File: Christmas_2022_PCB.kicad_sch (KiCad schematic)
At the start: 32 parts, among them J2 SOP8_test_point, J3 SOP8_test_point

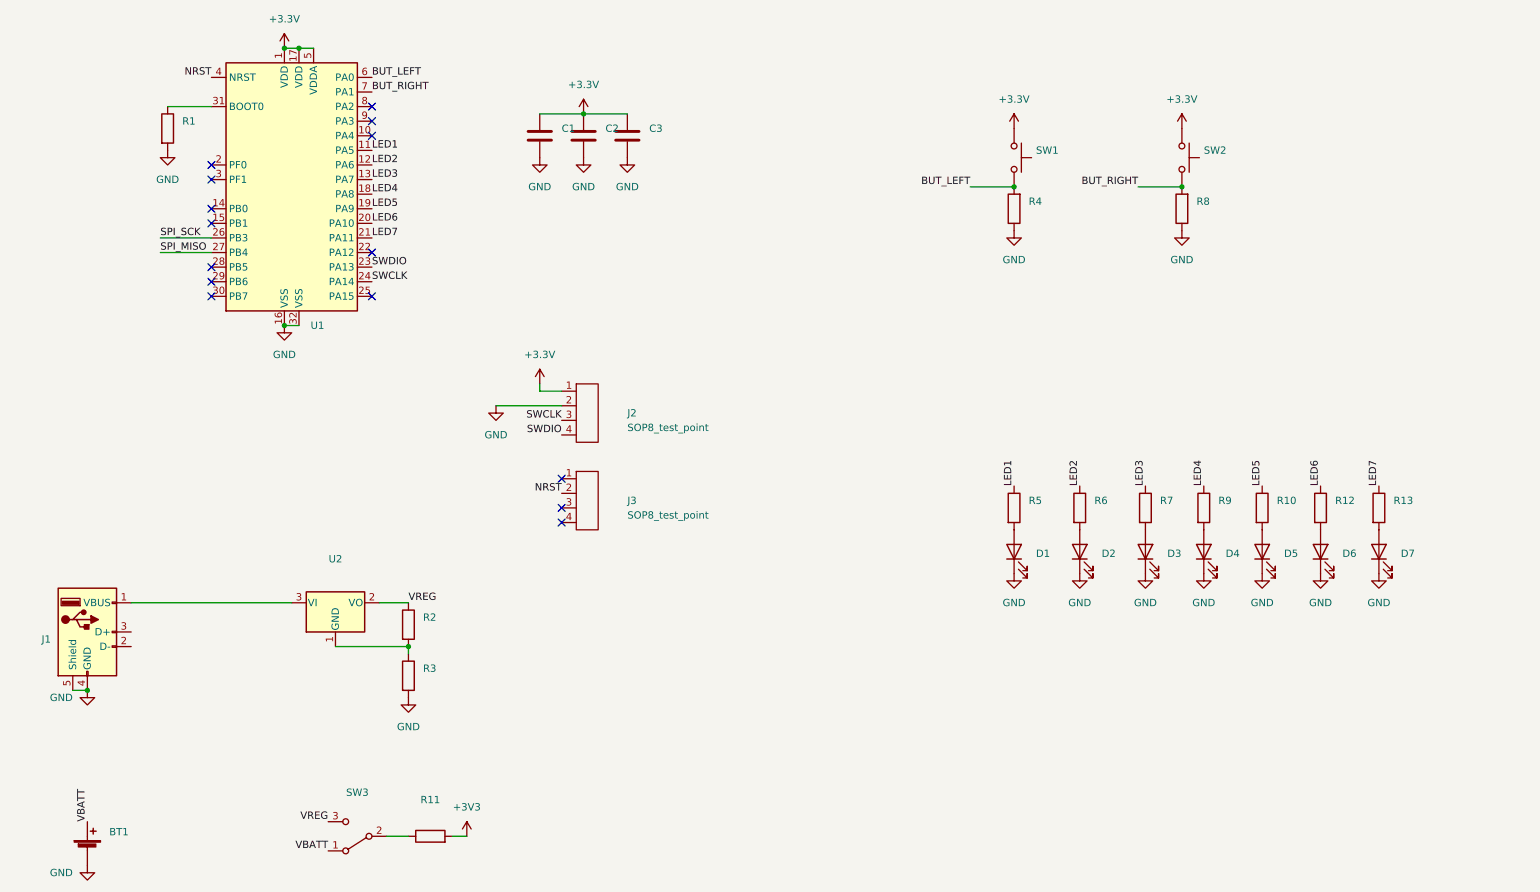
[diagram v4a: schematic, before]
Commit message: Added secondary LEDs
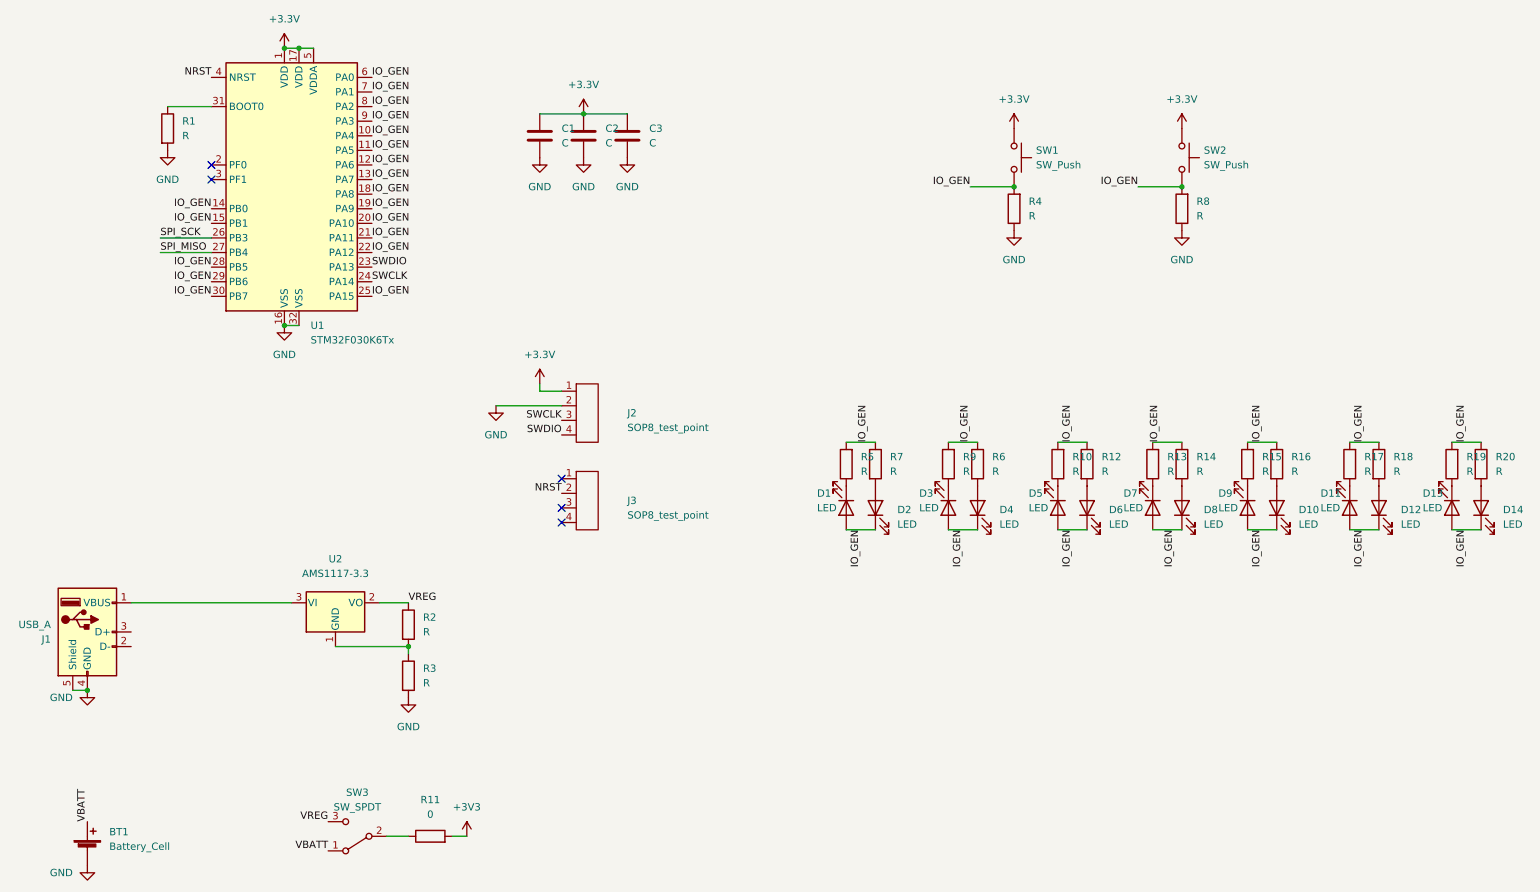
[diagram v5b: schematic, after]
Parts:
- added D10, D11, D12, D13, D14, D8, D9: LED, LED_SMD:LED_0805_2012Metric_Pad1.15x1.40mm_HandSolder, symbol Device:LED
- added R14, R15, R16, R17, R18, R19, R20: R, Resistor_SMD:R_0805_2012Metric_Pad1.20x1.40mm_HandSolder, symbol Device:R
- BT1: value (none) -> Battery_Cell; footprint (none) -> Battery:BatteryHolder_Keystone_3034_1x20mm
- C1, C2, C3: value (none) -> C; footprint (none) -> Capacitor_SMD:C_0805_2012Metric_Pad1.18x1.45mm_HandSolder
- D1, D2, D3, D4, D5, D6, D7: value (none) -> LED; footprint (none) -> LED_SMD:LED_0805_2012Metric_Pad1.15x1.40mm_HandSolder
- J1: value (none) -> USB_A; footprint (none) -> Connector_USB:USB_A_CNCTech_1001-011-01101_Horizontal
- R1, R10, R12, R13, R2, R3, R4, R5, R6, R7, R8, R9: value (none) -> R; footprint (none) -> Resistor_SMD:R_0805_2012Metric_Pad1.20x1.40mm_HandSolder
- R11: value (none) -> 0; footprint (none) -> Resistor_SMD:R_0805_2012Metric_Pad1.20x1.40mm_HandSolder
- SW1, SW2: value (none) -> SW_Push; footprint (none) -> Library:3_6_2_5mm_push_button_G_lead
- SW3: value (none) -> SW_SPDT; footprint (none) -> Button_Switch_SMD:SW_SPDT_PCM12
- U1: value (none) -> STM32F030K6Tx; footprint (none) -> Package_QFP:LQFP-32_7x7mm_P0.8mm
- U2: value (none) -> AMS1117-3.3; footprint (none) -> Package_TO_SOT_SMD:SOT-223-3_TabPin2
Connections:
- net BUT_LEFT is gone; now on net IO_GEN: R4.2, SW1.2, U1.6 (PA0)
- net BUT_RIGHT is gone; now on net IO_GEN: R8.2, SW2.2, U1.7 (PA1)
- net LED2 is gone; now on net IO_GEN: R6.1, U1.12 (PA6)
- net LED3 is gone; now on net IO_GEN: R7.1, U1.13 (PA7)
- net LED6 is gone; now on net IO_GEN: R12.1, U1.20 (PA10)
- net GND: no longer D1.1 (K), D2.1 (K), D3.1 (K), D4.1 (K), D5.1 (K), D6.1 (K), D7.1 (K)
- net at R6.2: now also D4.2 (A); no longer D2.2 (A)
- net IO_GEN: now reaches D5.2 (A), R10.2
- net IO_GEN: now also D1.2 (A), D2.1 (K), D3.2 (A), D4.1 (K), D6.1 (K), D7.2 (A), R13.2, R5.2, R9.2, U1.10 (PA4), U1.11 (PA5), U1.14 (PB0), U1.15 (PB1), U1.18 (PA8), U1.19 (PA9), U1.21 (PA11), U1.22 (PA12), U1.25 (PA15), U1.28 (PB5), U1.29 (PB6), U1.30 (PB7), U1.8 (PA2), U1.9 (PA3), D10.1 (K), D11.2 (A), D12.1 (K), D13.2 (A), D14.1 (K), D8.1 (K), D9.2 (A), R14.1, R15.2, R16.1, R17.2, R18.1, R19.2, R20.1
- net at R7.2: now also D2.2 (A); no longer D3.2 (A)
- net LED1: no longer names the net of R5.1
- net LED1: now also D1.1 (K); no longer U1.11 (PA5)
- net LED4: no longer names the net of R9.1
- net LED4: now also D3.1 (K); no longer U1.18 (PA8)
- net LED5: no longer names the net of R10.1
- net LED5: now also D5.1 (K); no longer U1.19 (PA9)
- net LED7: no longer names the net of R13.1
- net LED7: now also D7.1 (K); no longer U1.21 (PA11)
- new net: D14.2 (A), R20.2
- new net: D10.2 (A), R16.2
- new net: D9.1 (K), R15.1
- new net: D13.1 (K), R19.1
- new net: D11.1 (K), R17.1
- new net: D8.2 (A), R14.2
- new net: D12.2 (A), R18.2
- no-connect marks 15 -> 5

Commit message: finished routing. Added missing 3D models
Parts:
- removed R2, R3: R, Resistor_SMD:R_0805_2012Metric_Pad1.20x1.40mm_HandSolder, symbol Device:R
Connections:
- net GND: now also U2.1 (GND)
- removed net IO_GEN: D1.2 (A), D10.1 (K), D11.2 (A), D12.1 (K), D13.2 (A), D14.1 (K), D2.1 (K), D3.2 (A), D4.1 (K), D5.2 (A), D6.1 (K), D7.2 (A), D8.1 (K), D9.2 (A), R10.2, R12.1, R13.2, R14.1, R15.2, R16.1, R17.2, R18.1, R19.2, R20.1, R4.2, R5.2, R6.1, R7.1, R8.2, R9.2, SW1.2, SW2.2, U1.10 (PA4), U1.11 (PA5), U1.12 (PA6), U1.13 (PA7), U1.14 (PB0), U1.15 (PB1), U1.18 (PA8), U1.19 (PA9), U1.20 (PA10), U1.21 (PA11), U1.22 (PA12), U1.25 (PA15), U1.28 (PB5), U1.29 (PB6), U1.30 (PB7), U1.6 (PA0), U1.7 (PA1), U1.8 (PA2), U1.9 (PA3)
- new net LED1: R5.2, R7.1, U1.21 (PA11)
- new net LED10: D10.1 (K), D9.2 (A), U1.13 (PA7)
- new net LED11: R17.2, R18.1, U1.7 (PA1)
- new net LED12: D11.2 (A), D12.1 (K), U1.6 (PA0)
- new net LED13: R19.2, R20.1, U1.10 (PA4)
- new net LED14: D13.2 (A), D14.1 (K), U1.11 (PA5)
- new net LED2: D1.2 (A), D2.1 (K), U1.22 (PA12)
- new net LED3: R6.1, R9.2, U1.28 (PB5)
- new net LED4: D3.2 (A), D4.1 (K), U1.25 (PA15)
- new net LED5: R10.2, R12.1, U1.15 (PB1)
- new net LED6: D5.2 (A), D6.1 (K), U1.14 (PB0)
- new net LED7: R13.2, R14.1, U1.30 (PB7)
- new net LED8: D7.2 (A), D8.1 (K), U1.29 (PB6)
- new net LED9: R15.2, R16.1, U1.12 (PA6)
- new net SW_LEFT: R4.2, SW1.2, U1.8 (PA2)
- new net SW_RIGHT: R8.2, SW2.2, U1.9 (PA3)
- no-connect marks 5 -> 8

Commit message: Finished routing. Output gerbers and drill files
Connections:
- no-connect marks 8 -> 10
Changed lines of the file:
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@@
   (no_connect (at 78.74 63.5))
   (no_connect (at 78.74 66.04))
+  (no_connect (at 36.83 137.16))
+  (no_connect (at 36.83 139.7))
   (wire (pts (xy 29.21 147.32) (xy 26.67 147.32))
     (stroke (width 0) (type default) (color 0 0 0 0))
